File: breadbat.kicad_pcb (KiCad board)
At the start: 2 copper layers, 51.2 x 19.7 mm, 31 parts, among them J1 USB_C_Receptacle_PowerOnly_6P, J2 Conn_02x03_Odd_Even, J3 Conn_02x03_Odd_Even, U1 TP4056-42-ESOP8, U2 AMS1117-3.3, U3 TPS259621

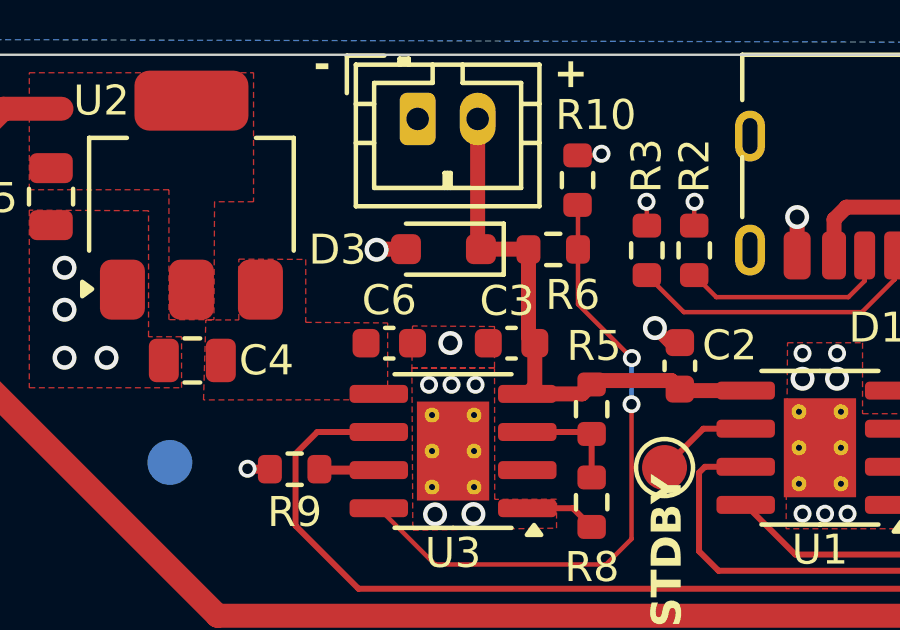
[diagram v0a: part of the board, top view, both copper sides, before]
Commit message: Added README
Added readme and added a BOM
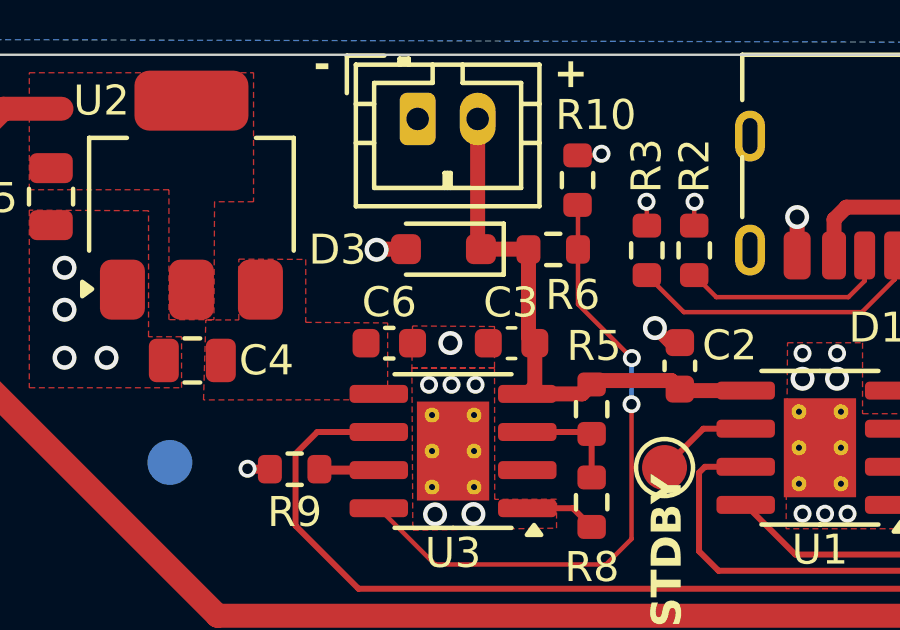
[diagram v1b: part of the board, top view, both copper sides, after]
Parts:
- C3: value 100n -> 1u
